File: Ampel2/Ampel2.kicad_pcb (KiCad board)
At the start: 2 copper layers, 27.9 x 33 mm, 19 parts, among them J1 Conn_01x07_Male, J2 Conn_01x07_Male, J3 Conn_01x03_Male, J4 Conn_01x03_Male, J5 AVR-ISP-6, Q1 BC 818-25, Q2 BC 818-25, U1 ATtiny85-20PU

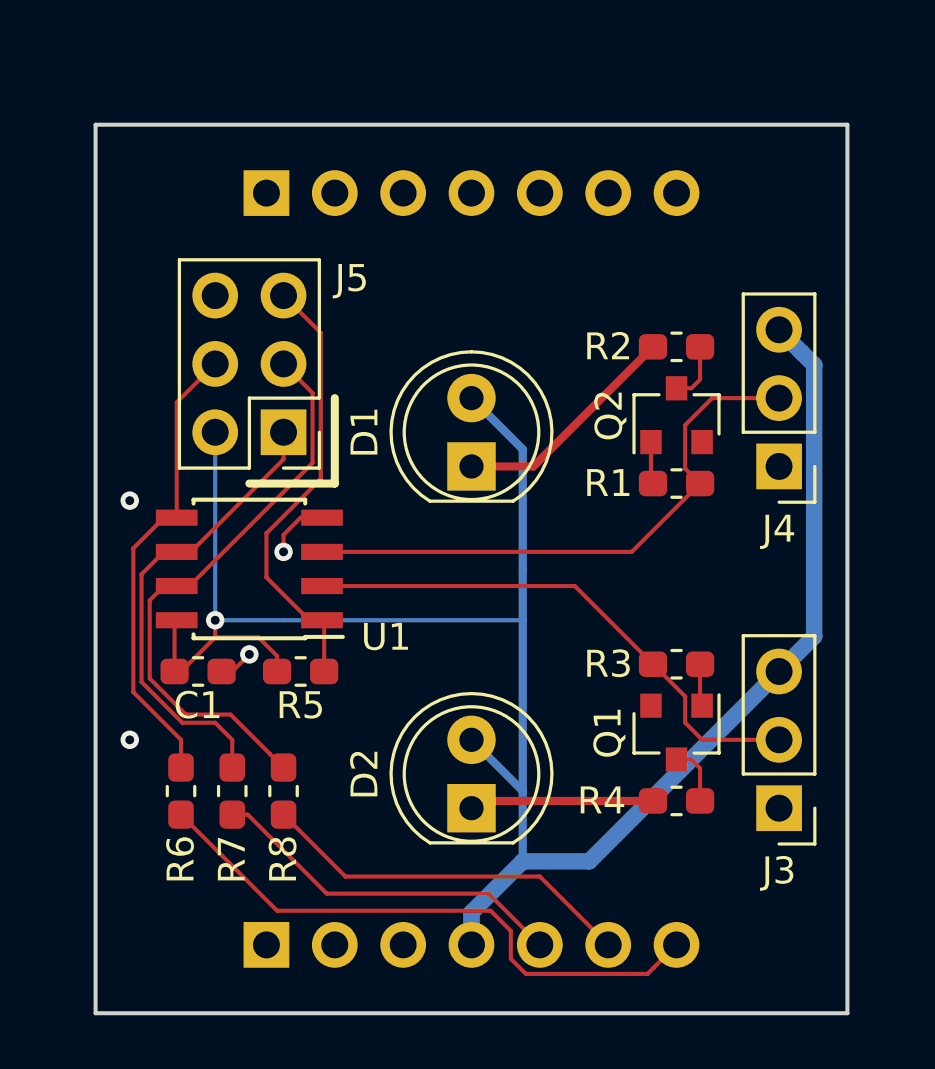
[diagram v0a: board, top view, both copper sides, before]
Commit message: Fix dimensions
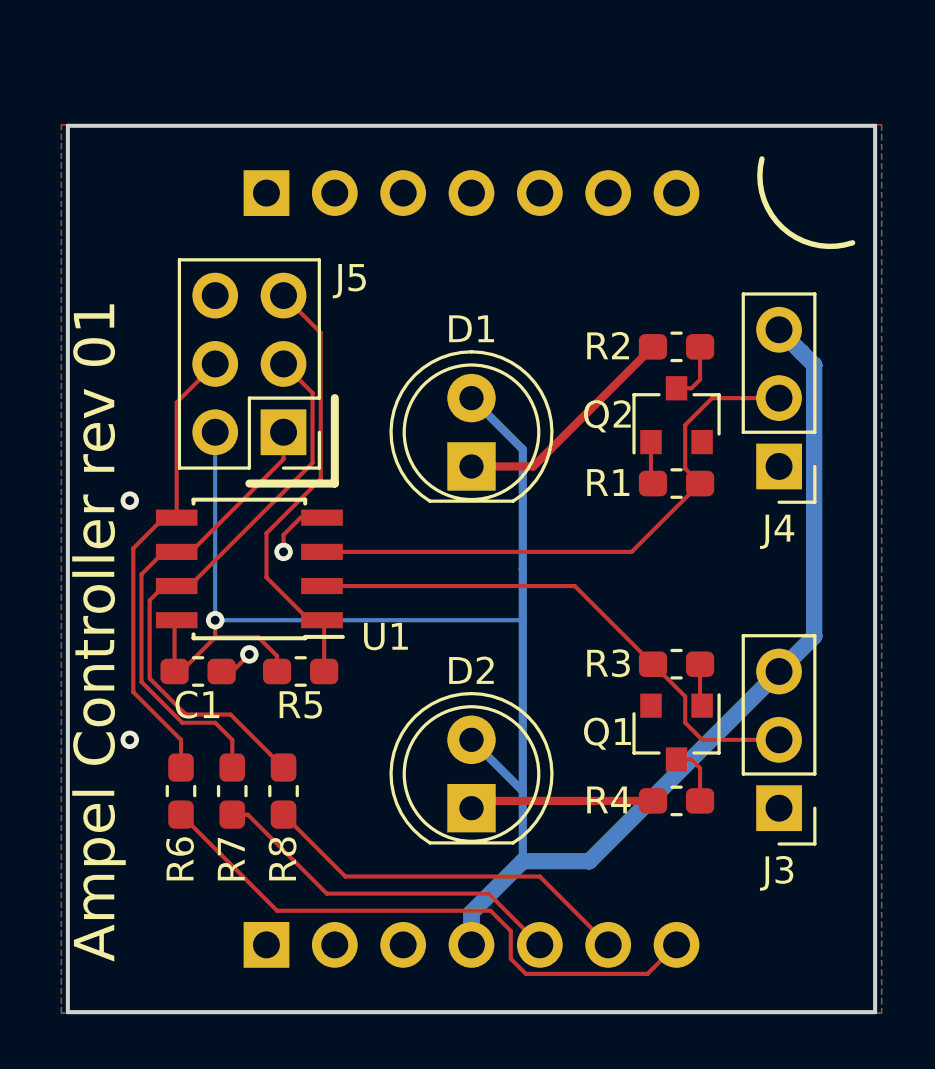
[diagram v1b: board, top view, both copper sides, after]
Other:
- board size 27.9 x 33 mm -> 30 x 32.9 mm
- board text added: "Ampel Controller rev 01"
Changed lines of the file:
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@@
   (general
     (thickness 1.6)
-    (drawings 6)
+    (drawings 8)
     (tracks 116)
     (zones 0)
@@
     (tags SOT-23)
     (attr smd)
-    (fp_text reference Q1 (at 0 2.54 270) (layer F.SilkS)
+    (fp_text reference Q1 (at 0 2.54) (layer F.SilkS)
       (effects (font (size 1 1) (thickness 0.15)))
     )
@@
     (tags SOT-23)
     (attr smd)
-    (fp_text reference Q2 (at 0 -2.5 90) (layer F.SilkS)
+    (fp_text reference Q2 (at 0 -2.54 180) (layer F.SilkS)
       (effects (font (size 1 1) (thickness 0.15)))
     )
@@
     (tags "resistor handsolder")
     (attr smd)
-    (fp_text reference R4 (at -2.78 0) (layer F.SilkS)
+    (fp_text reference R4 (at -2.54 0) (layer F.SilkS)
       (effects (font (size 1 1) (thickness 0.15)))
     )
@@
     (descr "LED, diameter 5.0mm, 2 pins, http://cdn-reichelt.de/documents/datenblatt/A500/LL-504BC2E-009.pdf")
     (tags "LED diameter 5.0mm 2 pins")
-    (fp_text reference D1 (at 1.27 -3.96 90) (layer F.SilkS)
+    (fp_text reference D1 (at 5.08 0 180) (layer F.SilkS)
       (effects (font (size 1 1) (thickness 0.15)))
     )
@@
     (descr "LED, diameter 5.0mm, 2 pins, http://cdn-reichelt.de/documents/datenblatt/A500/LL-504BC2E-009.pdf")
     (tags "LED diameter 5.0mm 2 pins")
-    (fp_text reference D2 (at 1.27 -3.96 90) (layer F.SilkS)
+    (fp_text reference D2 (at 5.08 0 180) (layer F.SilkS)
       (effects (font (size 1 1) (thickness 0.15)))
     )
@@
     )
   )
-  (gr_line (start 219.71 134.62) (end 219.71 101.6) (layer Edge.Cuts) (width 0.15))
-  (gr_line (start 247.65 134.62) (end 219.71 134.62) (layer Edge.Cuts) (width 0.15))
-  (gr_line (start 247.65 101.6) (end 247.65 134.62) (layer Edge.Cuts) (width 0.15))
-  (gr_line (start 219.71 101.6) (end 247.65 101.6) (layer Edge.Cuts) (width 0.15))
+  (gr_text "Ampel Controller rev 01" (at 219.71 132.715 90) (layer F.SilkS)
+    (effects (font (size 1.5 1.5) (thickness 0.1)) (justify left))
+  )
+  (gr_arc (start 247.015 103.505) (end 244.475001 102.870001) (angle -122.4711923) (layer F.SilkS) (width 0.2))
+  (gr_line (start 218.68 134.58) (end 218.68 101.64) (layer Edge.Cuts) (width 0.15))
+  (gr_line (start 248.68 134.58) (end 218.68 134.58) (layer Edge.Cuts) (width 0.15))
+  (gr_line (start 248.68 101.64) (end 248.68 134.58) (layer Edge.Cuts) (width 0.15))
+  (gr_line (start 218.68 101.64) (end 248.68 101.64) (layer Edge.Cuts) (width 0.15))
   (gr_line (start 228.6 114.935) (end 228.6 111.76) (layer F.SilkS) (width 0.3))
   (gr_line (start 225.425 114.935) (end 228.6 114.935) (layer F.SilkS) (width 0.3))
@@
   (segment (start 221.416589 122.306837) (end 221.416589 118.308411) (width 0.1524) (layer F.Cu) (net 17))
   (segment (start 224.155 123.825) (end 222.934752 123.825) (width 0.1524) (layer F.Cu) (net 17))
+  (zone (net 1) (net_name GND) (layer B.Cu) (hatch edge 0.508)
+    (connect_pads (clearance 0.508))
+    (min_thickness 0.254)
+    (fill yes (arc_segments 16) (thermal_gap 0.508) (thermal_bridge_width 0.508))
+    (polygon
+      (pts
+        (xy 218.44 101.6) (xy 248.92 101.6) (xy 248.92 134.62) (xy 218.44 134.62)
+      )
+    )
+  )
   (zone (net 1) (net_name GND) (layer F.Cu) (hatch edge 0.508)
     (connect_pads (clearance 0.508))
@@
     (polygon
       (pts
-        (xy 219.71 101.6) (xy 247.65 101.6) (xy 247.65 134.62) (xy 219.71 134.62)
+        (xy 218.44 101.6) (xy 248.92 101.6) (xy 248.92 134.62) (xy 218.44 134.62)
       )
     )
-  )
-  (zone (net 1) (net_name GND) (layer B.Cu) (hatch edge 0.508)
-    (connect_pads (clearance 0.508))
-    (min_thickness 0.254)
-    (fill yes (arc_segments 16) (thermal_gap 0.508) (thermal_bridge_width 0.508))
-    (polygon
-      (pts
-        (xy 219.71 101.6) (xy 247.65 101.6) (xy 247.65 134.62) (xy 219.71 134.62)
-      )
-    )

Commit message: Outline and mounting holes
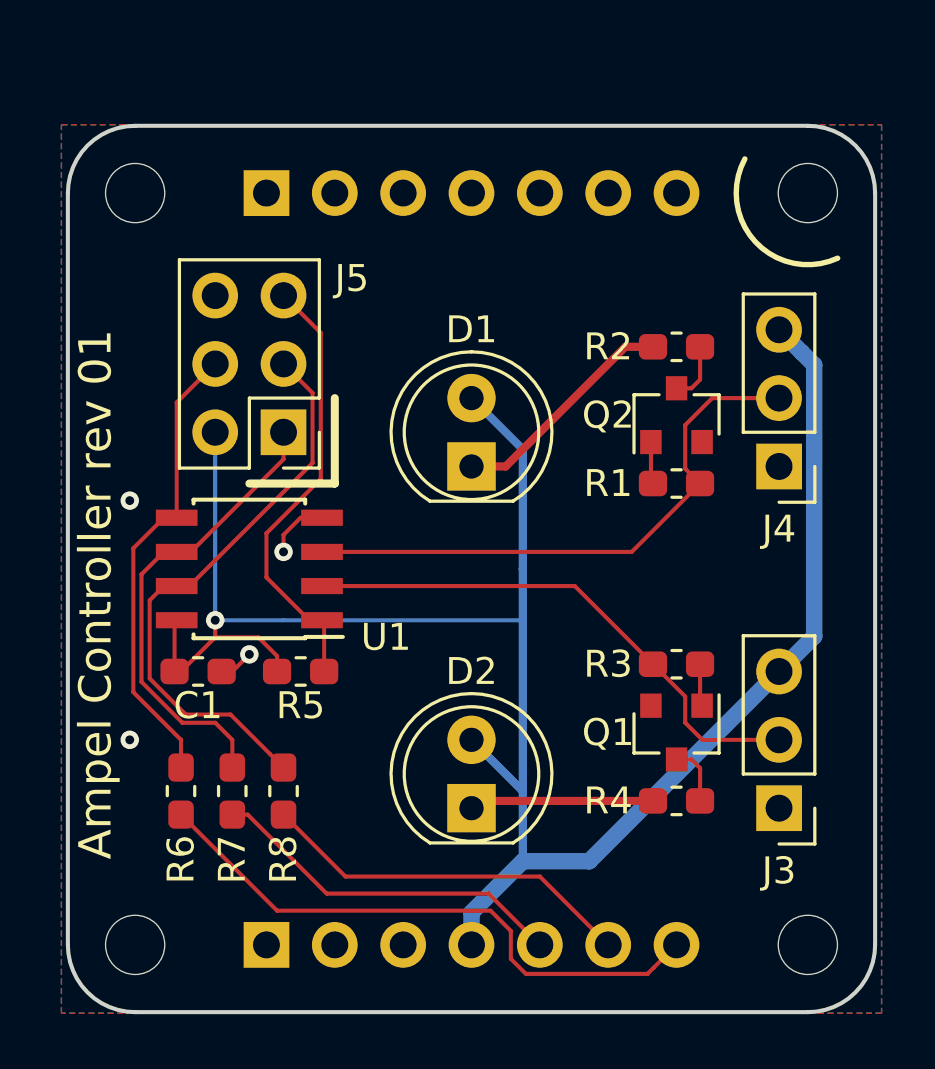
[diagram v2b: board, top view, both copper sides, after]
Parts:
- added MK1: 2.0, MountingHole:MountingHole_2.2mm_M2_DIN965, F.Cu at (221.2, 104.1)
- added MK2: 2.0, MountingHole:MountingHole_2.2mm_M2_DIN965, F.Cu at (221.2, 132.1)
- added MK3: 2.0, MountingHole:MountingHole_2.2mm_M2_DIN965, F.Cu at (246.2, 104.1)
- added MK4: 2.0, MountingHole:MountingHole_2.2mm_M2_DIN965, F.Cu at (246.2, 132.1)
- R2, R4: value 150R -> 100R
- R6, R7, R8: value 33R -> 10R
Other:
- outline, holes or cut-outs redrawn

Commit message: Move upper LED
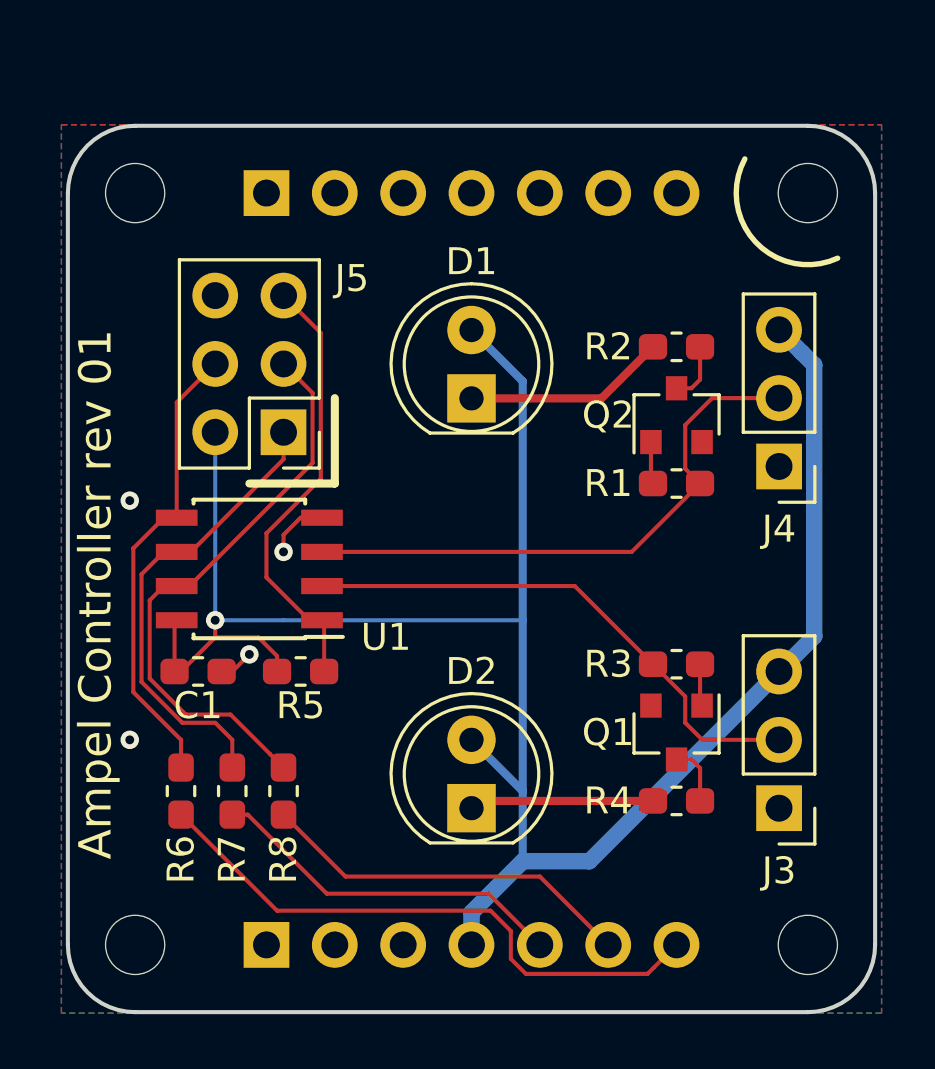
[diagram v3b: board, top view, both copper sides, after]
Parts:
- moved D1 2.53 mm to (233.7, 111.8)
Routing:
- net +5V: track 77.0 -> 79.5 mm
- net Net-(D1-Pad1): track 8.59 -> 7.54 mm
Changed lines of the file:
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@@
     (thickness 1.6)
     (drawings 12)
-    (tracks 117)
+    (tracks 115)
     (zones 0)
     (modules 23)
@@
   )
   (module LED_THT:LED_D5.0mm (layer F.Cu)
-    (at 233.68 114.3 90)
+    (at 233.68 111.77 90)
     (descr "LED, diameter 5.0mm, 2 pins, http://cdn-reichelt.de/documents/datenblatt/A500/LL-504BC2E-009.pdf")
     (tags "LED diameter 5.0mm 2 pins")
@@
   (segment (start 235.585 128.972919) (end 235.585 126.365) (width 0.3048) (layer B.Cu) (net 2))
   (segment (start 235.585 126.365) (end 233.68 124.46) (width 0.3048) (layer B.Cu) (net 2) (status 20))
-  (segment (start 235.585 113.665) (end 233.68 111.76) (width 0.3048) (layer B.Cu) (net 2) (status 20))
-  (segment (start 235.585 118.11) (end 235.585 113.665) (width 0.3048) (layer B.Cu) (net 2))
-  (segment (start 235.585 120.015) (end 235.585 118.11) (width 0.3048) (layer B.Cu) (net 2))
   (segment (start 235.585 126.365) (end 235.585 120.015) (width 0.3048) (layer B.Cu) (net 2))
   (segment (start 233.68 130.877919) (end 235.585 128.972919) (width 0.6096) (layer B.Cu) (net 2))
@@
   (segment (start 226.455 121.345) (end 225.76 120.65) (width 0.1524) (layer F.Cu) (net 2))
   (segment (start 226.455 121.92) (end 226.455 121.345) (width 0.1524) (layer F.Cu) (net 2) (status 10))
+  (segment (start 235.585 111.135) (end 233.68 109.23) (width 0.3048) (layer B.Cu) (net 2))
+  (segment (start 235.585 120.015) (end 235.585 111.135) (width 0.3048) (layer B.Cu) (net 2))
   (segment (start 234.315 130.175) (end 236.22 132.08) (width 0.1524) (layer F.Cu) (net 3) (status 20))
   (segment (start 228.3 130.175) (end 234.315 130.175) (width 0.1524) (layer F.Cu) (net 3))
@@
   (segment (start 241.621399 122.846399) (end 241.621399 123.822881) (width 0.1524) (layer F.Cu) (net 10))
   (segment (start 240.425 121.65) (end 241.621399 122.846399) (width 0.1524) (layer F.Cu) (net 10) (status 10))
-  (segment (start 239.395 109.855) (end 240.425 109.855) (width 0.3048) (layer F.Cu) (net 11))
-  (segment (start 234.95 114.3) (end 239.395 109.855) (width 0.3048) (layer F.Cu) (net 11))
-  (segment (start 233.68 114.3) (end 234.95 114.3) (width 0.3048) (layer F.Cu) (net 11))
+  (segment (start 238.51 111.77) (end 240.425 109.855) (width 0.3048) (layer F.Cu) (net 11) (status 1000000))
+  (segment (start 233.68 111.77) (end 238.51 111.77) (width 0.3048) (layer F.Cu) (net 11) (status 1000000))
   (segment (start 239.635 117.475) (end 242.175 114.935) (width 0.1524) (layer F.Cu) (net 12) (status 20))
   (segment (start 228.125 117.475) (end 239.635 117.475) (width 0.1524) (layer F.Cu) (net 12) (status 10))

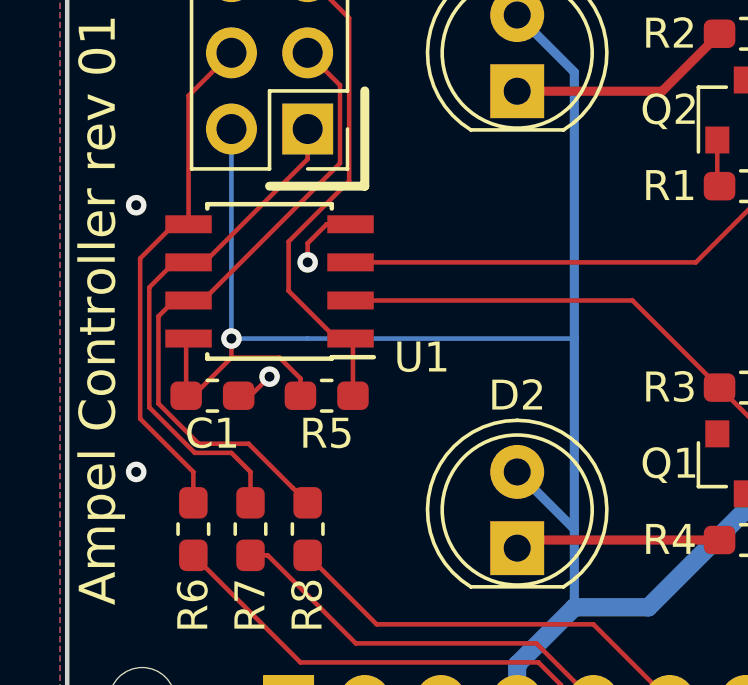
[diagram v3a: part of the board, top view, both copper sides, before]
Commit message: Fix Attiny85 footprint
Change to the attiny we actually have (Attiny85V-10 SU)
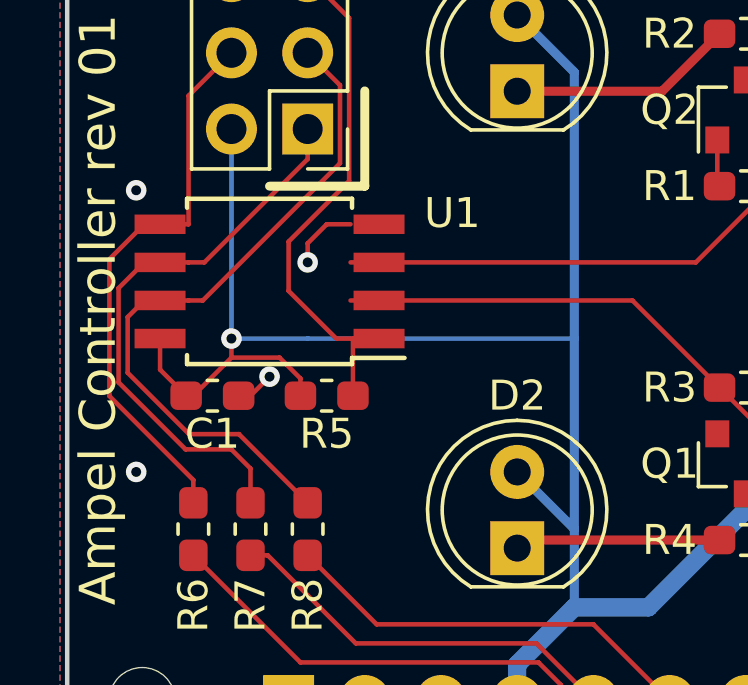
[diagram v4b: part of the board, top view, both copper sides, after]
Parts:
- U1: value ATtiny85-20PU -> ATtiny85V-10SU; footprint Package_SO:SOIC-8_3.9x4.9mm_P1.27mm -> Package_SO:SOIJ-8_5.3x5.3mm_P1.27mm
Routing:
- net ISP_MISO: track 17.3 -> 18.5 mm
- net ISP_SCK: track 21.5 -> 22.5 mm
- net ISP_MOSI: track 17.3 -> 18.2 mm
- net ISP_RST: track 16.5 -> 17.5 mm
